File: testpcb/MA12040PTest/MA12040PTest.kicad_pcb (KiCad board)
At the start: 2 copper layers, 110 parts, among them J1 24v Input, J2 USB4085-GF-A_REVB, J3 Screw_Terminal_01x04, Q1 DMP3013SFV-7, U1 AP64501SP-13, U10 PCM5101A, U11 CP2615-xx-xM, U2 FSUSB42MUX, U3 LT1761-3.3, U4 LT1761-3.3, U5 74LVC1G07SE-7, U6 74LVC1G07SE-7, U7 74LVC1G07SE-7, U8 74LVC1G07SE-7, U9 MA12040PXUMA1

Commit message: - work in progress
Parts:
- removed the C18 at (32.0, 98.7)
- removed the U3 at (27.2, 98.7)
- added C26: 1u, Capacitor_SMD:C_0805_2012Metric_Pad1.18x1.45mm_HandSolder, F.Cu at (155.6, 97.2)
- added C27: 22p, Capacitor_SMD:C_0805_2012Metric_Pad1.18x1.45mm_HandSolder, F.Cu at (190.5, 97.1)
- added C28: 22p, Capacitor_SMD:C_0805_2012Metric_Pad1.18x1.45mm_HandSolder, F.Cu at (190.5, 100.1)
- added C29: 1u, Capacitor_SMD:C_0805_2012Metric_Pad1.18x1.45mm_HandSolder, F.Cu at (155.6, 100.2)
- added C30: 100n, Capacitor_SMD:C_0805_2012Metric_Pad1.18x1.45mm_HandSolder, F.Cu at (201.2, 91.0)
- added C31: 100n, Capacitor_SMD:C_0805_2012Metric_Pad1.18x1.45mm_HandSolder, F.Cu at (128.7, 69.2)
- added C36: 1u, Capacitor_SMD:C_0805_2012Metric_Pad1.18x1.45mm_HandSolder, F.Cu at (128.7, 72.2)
- added C37: 100n, Capacitor_SMD:C_0805_2012Metric_Pad1.18x1.45mm_HandSolder, F.Cu at (128.7, 75.2)
- added C38: 100n, Capacitor_SMD:C_0805_2012Metric_Pad1.18x1.45mm_HandSolder, F.Cu at (128.7, 78.2)
- added C39: 100n, Capacitor_SMD:C_0805_2012Metric_Pad1.18x1.45mm_HandSolder, F.Cu at (128.7, 81.2)
- added C47: 100n, Capacitor_SMD:C_0805_2012Metric_Pad1.18x1.45mm_HandSolder, F.Cu at (128.7, 84.2)
- added C53: 100n, Capacitor_SMD:C_0805_2012Metric_Pad1.18x1.45mm_HandSolder, F.Cu at (128.7, 87.2)
- added J3: Conn_02x03_Top_Bottom, Connector_PinHeader_2.54mm:PinHeader_2x03_P2.54mm_Vertical, F.Cu at (156.1, 107.3)
- added JP1: USB-VBUS, Jumper:SolderJumper-2_P1.3mm_Bridged_Pad1.0x1.5mm, F.Cu at (63.8, 62.3)
- added JP10: ~, Jumper:SolderJumper-2_P1.3mm_Open_TrianglePad1.0x1.5mm, F.Cu at (169.9, 113.3)
- added JP11: ~, Jumper:SolderJumper-2_P1.3mm_Open_TrianglePad1.0x1.5mm, F.Cu at (177.0, 113.3)
- added JP12: ~, Jumper:SolderJumper-2_P1.3mm_Open_TrianglePad1.0x1.5mm, F.Cu at (187.7, 113.3)
- added JP13: ~, Jumper:SolderJumper-2_P1.3mm_Open_TrianglePad1.0x1.5mm, F.Cu at (184.1, 113.3)
- added JP14: ~, Jumper:SolderJumper-2_P1.3mm_Open_TrianglePad1.0x1.5mm, F.Cu at (173.5, 113.3)
- added JP15: ~, Jumper:SolderJumper-2_P1.3mm_Open_TrianglePad1.0x1.5mm, F.Cu at (180.6, 113.3)
- added R17: 10k, Resistor_SMD:R_0805_2012Metric_Pad1.20x1.40mm_HandSolder, F.Cu at (201.2, 93.9)
- added R2: 1k5, Resistor_SMD:R_0805_2012Metric_Pad1.20x1.40mm_HandSolder, F.Cu at (59.3, 62.3)
- added R22: 1k, Resistor_SMD:R_0805_2012Metric_Pad1.20x1.40mm_HandSolder, F.Cu at (133.5, 85.4)
- added R23: 10k, Resistor_SMD:R_0805_2012Metric_Pad1.20x1.40mm_HandSolder, F.Cu at (133.5, 82.4)
- added R26: 1k5, Resistor_SMD:R_0805_2012Metric_Pad1.20x1.40mm_HandSolder, F.Cu at (197.7, 117.8)
- added R27: 1k5, Resistor_SMD:R_0805_2012Metric_Pad1.20x1.40mm_HandSolder, F.Cu at (197.7, 120.7)
- added R28: 1k5, Resistor_SMD:R_0805_2012Metric_Pad1.20x1.40mm_HandSolder, F.Cu at (197.7, 123.7)
- added R29: 1k5, Resistor_SMD:R_0805_2012Metric_Pad1.20x1.40mm_HandSolder, F.Cu at (202.5, 111.9)
- added R30: 1k5, Resistor_SMD:R_0805_2012Metric_Pad1.20x1.40mm_HandSolder, F.Cu at (202.5, 114.8)
- added R31: 1k5, Resistor_SMD:R_0805_2012Metric_Pad1.20x1.40mm_HandSolder, F.Cu at (202.5, 117.8)
- added R32: 1k5, Resistor_SMD:R_0805_2012Metric_Pad1.20x1.40mm_HandSolder, F.Cu at (202.5, 120.7)
- added R33: 1k5, Resistor_SMD:R_0805_2012Metric_Pad1.20x1.40mm_HandSolder, F.Cu at (202.5, 123.7)
- added R34: 1k5, Resistor_SMD:R_0805_2012Metric_Pad1.20x1.40mm_HandSolder, F.Cu at (207.2, 111.9)
- added R35: 1k5, Resistor_SMD:R_0805_2012Metric_Pad1.20x1.40mm_HandSolder, F.Cu at (207.2, 114.8)
- added R36: 1k5, Resistor_SMD:R_0805_2012Metric_Pad1.20x1.40mm_HandSolder, F.Cu at (207.2, 117.8)
- added R37: 1k5, Resistor_SMD:R_0805_2012Metric_Pad1.20x1.40mm_HandSolder, F.Cu at (207.2, 120.7)
- added TP21: Reset, TestPoint:TestPoint_Bridge_Pitch2.0mm_Drill0.7mm, F.Cu at (132.8, 69.4)
- added TP22: RP_SCL, TestPoint:TestPoint_Bridge_Pitch2.0mm_Drill0.7mm, F.Cu at (132.8, 72.8)
- added TP23: RP_SDA, TestPoint:TestPoint_Bridge_Pitch2.0mm_Drill0.7mm, F.Cu at (132.8, 76.3)
- added U12: AP2112K-3.3, Package_TO_SOT_SMD:SOT-23-5, F.Cu at (166.4, 98.5)
- added U13: RP2040, Package_DFN_QFN:QFN-56-1EP_7x7mm_P0.4mm_EP3.2x3.2mm, F.Cu at (178.3, 100.2)
- added U6: AP2112K-3.3, Package_TO_SOT_SMD:SOT-23-5, F.Cu at (120.4, 36.6)
- added U7: S25FL064LABMFI010, Footprints:SOIC8_208MIL_CYP, F.Cu at (178.0, 88.6)
- added Y1: 12Mhz, Crystal:Crystal_SMD_Abracon_ABM3-2Pin_5.0x3.2mm_HandSoldering, F.Cu at (186.1, 107.3)
- C12: renamed from C23; moved to B.Cu
- C14: renamed from C43; footprint Capacitor_SMD:CP_Elec_6.3x3.9 -> Capacitor_SMD:CP_Elec_5x5.8
- C15: renamed from C19; moved to B.Cu
- C17: renamed from C41; moved to B.Cu
- C21: renamed from C40; footprint Capacitor_SMD:CP_Elec_6.3x3.9 -> Capacitor_SMD:CP_Elec_5x5.8
- C23: renamed from C20; moved to B.Cu
- C24: renamed from C42; footprint Capacitor_SMD:CP_Elec_6.3x3.9 -> Capacitor_SMD:CP_Elec_5x5.8
- TP16: renamed from TP20; footprint TestPoint:TestPoint_Bridge_Pitch2.0mm_Drill0.7mm -> TestPoint:TestPoint_THTPad_1.0x1.0mm_Drill0.5mm
- TP9: renamed from TP13; footprint TestPoint:TestPoint_Bridge_Pitch2.0mm_Drill0.7mm -> TestPoint:TestPoint_THTPad_1.0x1.0mm_Drill0.5mm
- moved C25 111.7 mm to (120.5, 32.3)
- moved D2 63.6 mm to (53.4, 58.9), turned to 180 degrees
- moved TP14 62.6 mm to (94.4, 55.2)
- moved TP9 41.7 mm to (67.4, 62.6)
- moved R10 41.2 mm to (50.1, 64.4)
- moved R14 40.7 mm to (50.3, 67.8)
- moved C12 34.6 mm to (87.0, 106.3), turned to -90 degrees
- moved R6 34.4 mm to (90.9, 56.3)
- moved TP7 34.4 mm to (66.2, 53.6)
- moved R4 34.4 mm to (75.4, 68.7)
- moved TP10 34.4 mm to (75.3, 55.8)
- moved TP13 34.4 mm to (75.3, 58.9)
- moved TP3 34.4 mm to (59.5, 54.8)
- moved TP4 34.4 mm to (59.5, 57.8)
- moved TP6 34.4 mm to (62.9, 53.7)
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- renumbered C12 to C10, C7 to C11, C8 to C13, C22 to C16, C15 to C18, C16 to C19, C11 to C20, C13 to C22, C21 to C25, C24 to C32, C25 to C33, C26 to C34, C27 to C35, C9 to C4, C28 to C40, C29 to C41, C30 to C42, C31 to C43, C32 to C44, C33 to C45, C34 to C46, C35 to C48, C36 to C49, C10 to C5, C37 to C50, C38 to C51, C39 to C52, C4 to C6, C5 to C7, C6 to C8, C14 to C9, J3 to J4, JP1 to JP2, JP2 to JP3, JP3 to JP4, JP4 to JP6, JP11 to JP8, JP12 to JP9, R3 to R10, R7 to R11, R8 to R12, R12 to R13, R4 to R14, R14 to R16, R16 to R20, R17 to R21, R11 to R3, R10 to R4, R2 to R5, R5 to R6, R9 to R7, R6 to R8, R13 to R9, TP11 to TP1, TP7 to TP10, TP8 to TP11, TP9 to TP12, TP10 to TP13, TP18 to TP14, TP6 to TP15, TP14 to TP17, TP15 to TP18, TP16 to TP19, TP12 to TP2, TP17 to TP20, TP2 to TP3, TP3 to TP4, TP1 to TP5, TP4 to TP6, TP5 to TP7, TP19 to TP8, U4 to U1, U7 to U10, U8 to U11, U9 to U14, U1 to U3, U11 to U4, U10 to U5, U5 to U8, U6 to U9
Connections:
- net Net-(U11-I2C_SCL) renamed /PICO_SCL
- net Net-(U11-I2C_SDA) renamed /PICO_SDA
- net Net-(U11-~{CFGMODE}) renamed /CFGMODE
- net Net-(U11-~{RST}) renamed /SOUND_RESET
- D2 pad 4: Net-(U2-SEL) -> Net-(D2-K-Pad4)
- J2 pad A4: Net-(U2-SEL) -> Net-(D2-K-Pad4)
- J2 pad A9: Net-(U2-SEL) -> Net-(D2-K-Pad4)
- J2 pad B4: Net-(U2-SEL) -> Net-(D2-K-Pad4)
- J2 pad B9: Net-(U2-SEL) -> Net-(D2-K-Pad4)
- TP9 pad 1: Net-(U2-SEL) -> /USB_SEL
- U2 pad 2: Net-(U2-SEL) -> /USB_SEL
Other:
- board outline added: 182.2 x 115.9 mm

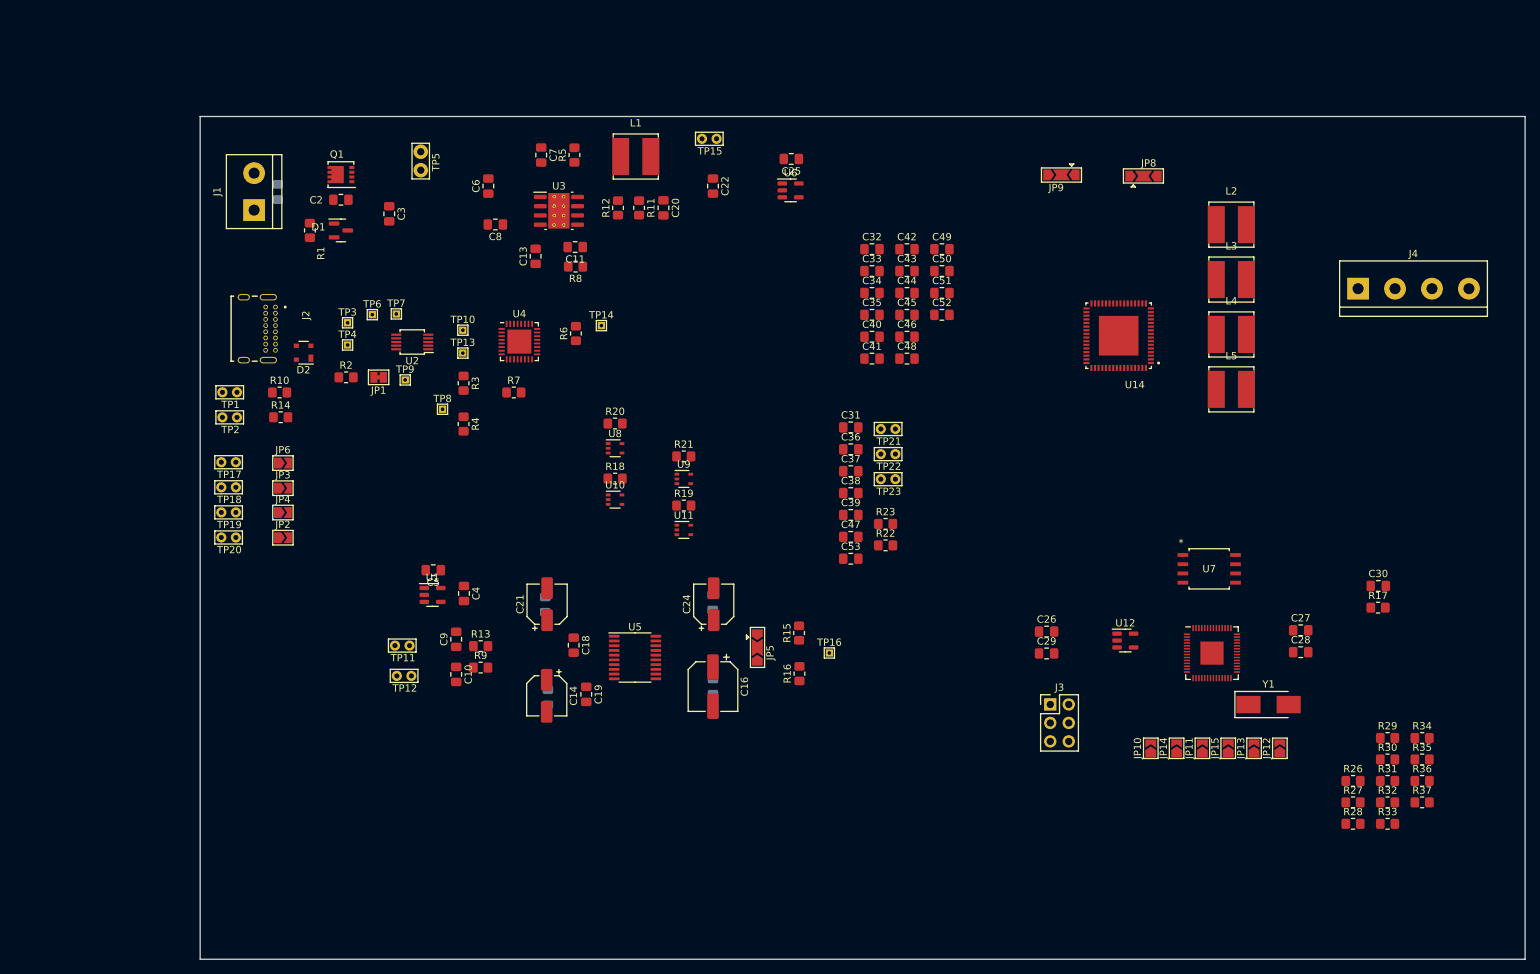
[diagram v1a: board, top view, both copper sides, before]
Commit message: - power routed, locked
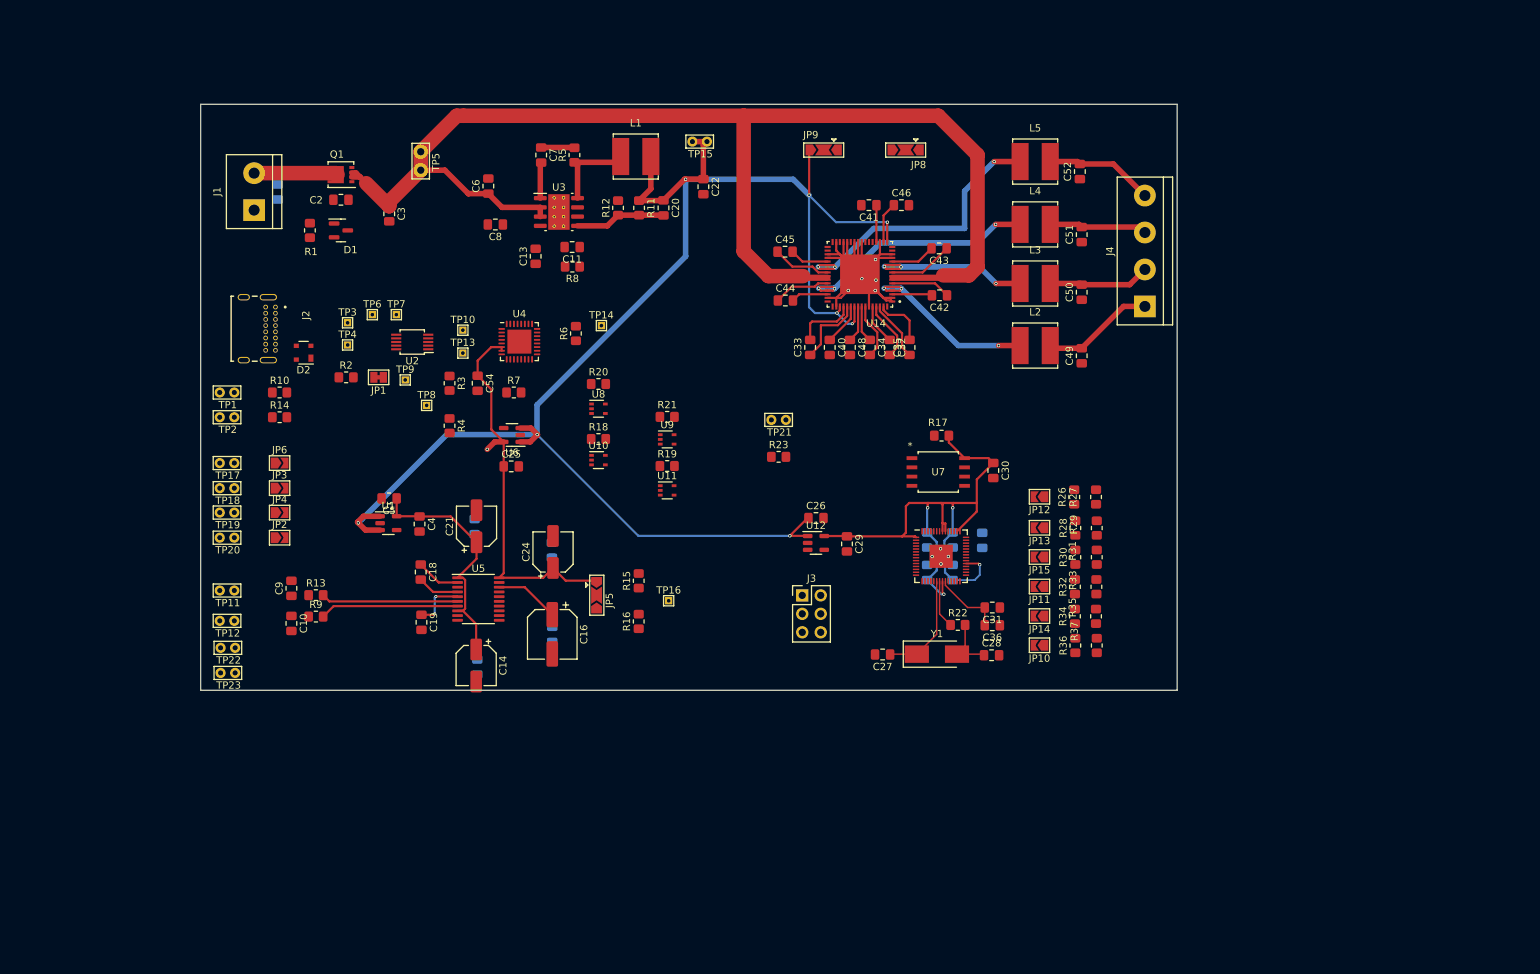
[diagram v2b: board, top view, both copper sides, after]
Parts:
- added C54: 1u, Capacitor_SMD:C_0805_2012Metric_Pad1.18x1.45mm_HandSolder, F.Cu at (77.4, 63.1)
- C37, C38, C39, C47, C53: moved to B.Cu
- moved TP22 94.6 mm to (42.0, 99.5)
- moved TP23 94.6 mm to (42.0, 102.9)
- moved R17 64.5 mm to (141.2, 70.3)
- moved C27 57.6 mm to (133.0, 100.4), turned to 180 degrees
- moved C25 57.2 mm to (82.0, 74.5), turned to 0 degrees
- moved R28 55.8 mm to (159.5, 83.0), turned to 90 degrees
- moved C30 55.3 mm to (148.3, 75.1), turned to -90 degrees
- moved R27 54.9 mm to (162.4, 78.7), turned to 90 degrees
- moved R26 54.7 mm to (159.4, 78.7), turned to 90 degrees
- moved R32 52.2 mm to (159.5, 91.1), turned to 90 degrees
- moved R33 51.6 mm to (162.4, 91.1), turned to 90 degrees
- moved R36 51.2 mm to (159.5, 99.2), turned to 90 degrees
- moved R30 51.2 mm to (159.5, 87.0), turned to 90 degrees
- moved U6 51.0 mm to (82.1, 70.2), turned to 180 degrees
- moved R34 50.6 mm to (159.5, 95.1), turned to 90 degrees
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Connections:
- C29 pad 1: Net-(U12-VOUT) -> /+Pico 3.3v
- C30 pad 1: /+3.3v -> /+Pico 3.3v
- C37 pad 1: /+3.3v -> /+Pico 3.3v
- C38 pad 1: /+3.3v -> /+Pico 3.3v
- C39 pad 1: /+3.3v -> /+Pico 3.3v
- C47 pad 1: /+3.3v -> /+Pico 3.3v
- C49 pad 2: Net-(J4-Pin_2) -> Net-(J4-Pin_1)
- C50 pad 2: Net-(J4-Pin_1) -> Net-(J4-Pin_2)
- C51 pad 2: Net-(J4-Pin_4) -> Net-(J4-Pin_3)
- C52 pad 2: Net-(J4-Pin_3) -> Net-(J4-Pin_4)
- C53 pad 1: /+3.3v -> /+Pico 3.3v
- J3 pad 5: Net-(J3-Pin_5) -> unconnected-(J3-Pin_5-Pad5)
- L2 pad 2: Net-(J4-Pin_2) -> Net-(J4-Pin_1)
- L3 pad 2: Net-(J4-Pin_1) -> Net-(J4-Pin_2)
- L4 pad 2: Net-(J4-Pin_4) -> Net-(J4-Pin_3)
- L5 pad 2: Net-(J4-Pin_3) -> Net-(J4-Pin_4)
- R17 pad 2: /+3.3v -> /+Pico 3.3v
- R23 pad 2: /+3.3v -> /+Pico 3.3v
- TP22 pad 1: Net-(U13-GPIO14) -> Net-(U13-GPIO22)
- TP23 pad 1: Net-(U13-GPIO15) -> Net-(U13-GPIO23)
- U12 pad 5: Net-(U12-VOUT) -> /+Pico 3.3v
- U13 pad 1: Net-(U12-VOUT) -> /+Pico 3.3v
- U13 pad 10: Net-(U12-VOUT) -> /+Pico 3.3v
- U13 pad 13: Net-(JP10-B) -> unconnected-(U13-GPIO10-Pad13)
- U13 pad 14: Net-(JP14-B) -> unconnected-(U13-GPIO11-Pad14)
- U13 pad 15: Net-(JP11-B) -> unconnected-(U13-GPIO12-Pad15)
- U13 pad 16: Net-(JP15-B) -> unconnected-(U13-GPIO13-Pad16)
- U13 pad 17: Net-(U13-GPIO14) -> unconnected-(U13-GPIO14-Pad17)
- U13 pad 18: Net-(U13-GPIO15) -> unconnected-(U13-GPIO15-Pad18)
- U13 pad 22: Net-(U12-VOUT) -> /+Pico 3.3v
- U13 pad 27: Net-(JP13-B) -> unconnected-(U13-GPIO16-Pad27)
- U13 pad 28: Net-(JP12-B) -> unconnected-(U13-GPIO17-Pad28)
- U13 pad 29: unconnected-(U13-GPIO18-Pad29) -> Net-(JP10-B)
- U13 pad 30: unconnected-(U13-GPIO19-Pad30) -> Net-(JP14-B)
- U13 pad 31: unconnected-(U13-GPIO20-Pad31) -> Net-(JP11-B)
- U13 pad 32: unconnected-(U13-GPIO21-Pad32) -> Net-(JP15-B)
- U13 pad 33: Net-(U12-VOUT) -> /+Pico 3.3v
- U13 pad 34: unconnected-(U13-GPIO22-Pad34) -> Net-(U13-GPIO22)
- U13 pad 35: unconnected-(U13-GPIO23-Pad35) -> Net-(U13-GPIO23)
- U13 pad 36: unconnected-(U13-GPIO24-Pad36) -> Net-(JP13-B)
- U13 pad 37: unconnected-(U13-GPIO25-Pad37) -> Net-(JP12-B)
- U13 pad 42: Net-(U12-VOUT) -> /+Pico 3.3v
- U13 pad 43: Net-(U12-VOUT) -> /+Pico 3.3v
- U13 pad 44: Net-(U12-VOUT) -> /+Pico 3.3v
- U13 pad 48: Net-(U12-VOUT) -> /+Pico 3.3v
- U13 pad 49: Net-(U12-VOUT) -> /+Pico 3.3v
- U7 pad 8: /+3.3v -> /+Pico 3.3v
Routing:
- net /+5v: track 0.00 -> 221.4 mm, vias 0 -> 8
- net /+12v: track 0.00 -> 198.8 mm
- net /+Pico 3.3v: track 0.00 -> 87.8 mm, vias 0 -> 4
- net GND: track 0.00 -> 76.3 mm, vias 0 -> 9
- net /+3.3v: track 0.00 -> 53.5 mm, vias 0 -> 1
- net Net-(L5-Pad1): track 0.00 -> 42.1 mm, vias 0 -> 3
- net Net-(L4-Pad1): track 0.00 -> 36.4 mm, vias 0 -> 3
- net Net-(U1-VOUT): track 0.00 -> 33.2 mm
- net Net-(L2-Pad1): track 0.00 -> 27.3 mm, vias 0 -> 3
- net Net-(L3-Pad1): track 0.00 -> 24.9 mm, vias 0 -> 3
- net Net-(U5-OUTR): track 0.00 -> 19.1 mm
- net Net-(U5-OUTL): track 0.00 -> 18.8 mm
- net Net-(J4-Pin_1): track 0.00 -> 15.5 mm
- net Net-(J4-Pin_4): track 0.00 -> 14.9 mm
- net Net-(U13-XIN): track 0.00 -> 14.8 mm
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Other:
- board size 182.2 x 115.9 mm -> 134.3 x 80.6 mm
